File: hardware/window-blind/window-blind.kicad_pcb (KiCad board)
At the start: 2 copper layers, 31 parts, among them IC1 ATMEGA48PA-A, P1 CONN_02X03, SW1 UP, SW2 DN, SW3 END1, SW4 END2, U1 SP3485CN, U2 L298N, U3 LM78L05ACZ, Y1 16M

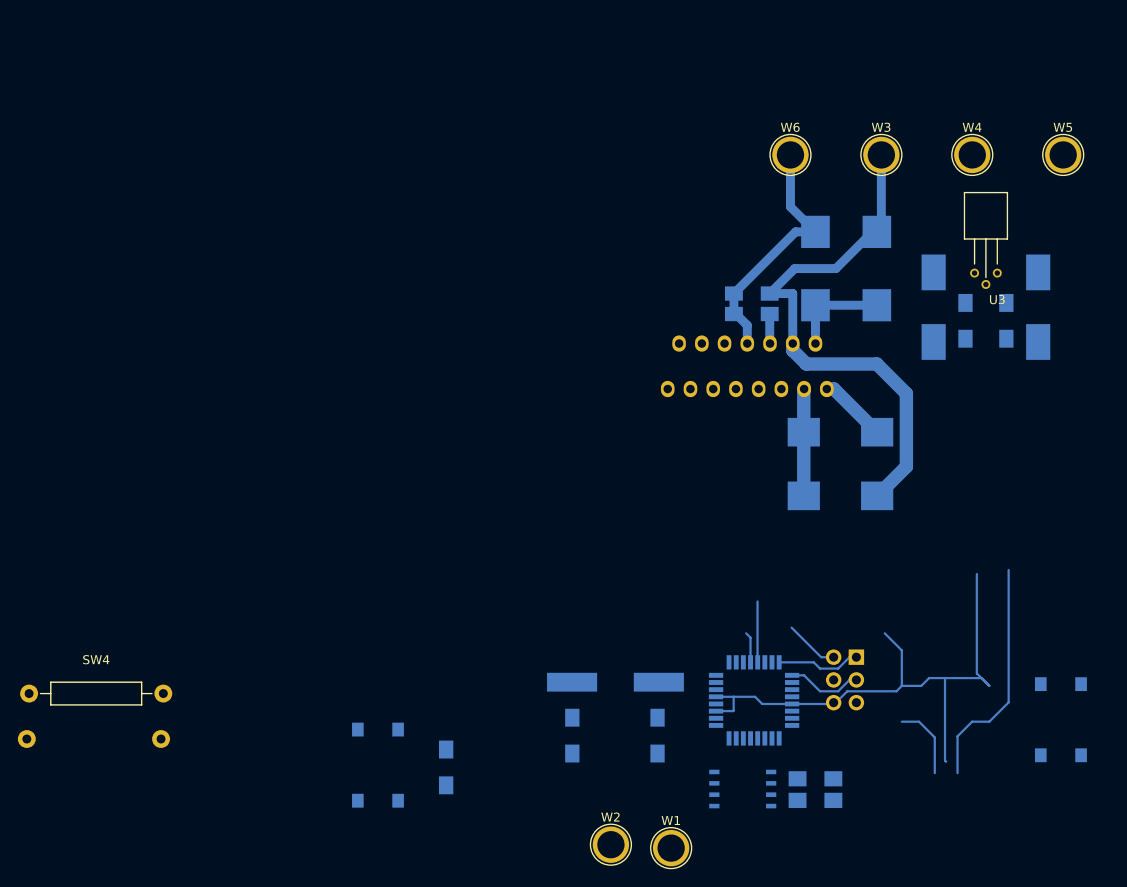
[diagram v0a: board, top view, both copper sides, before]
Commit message: Built sunblind PCB layout
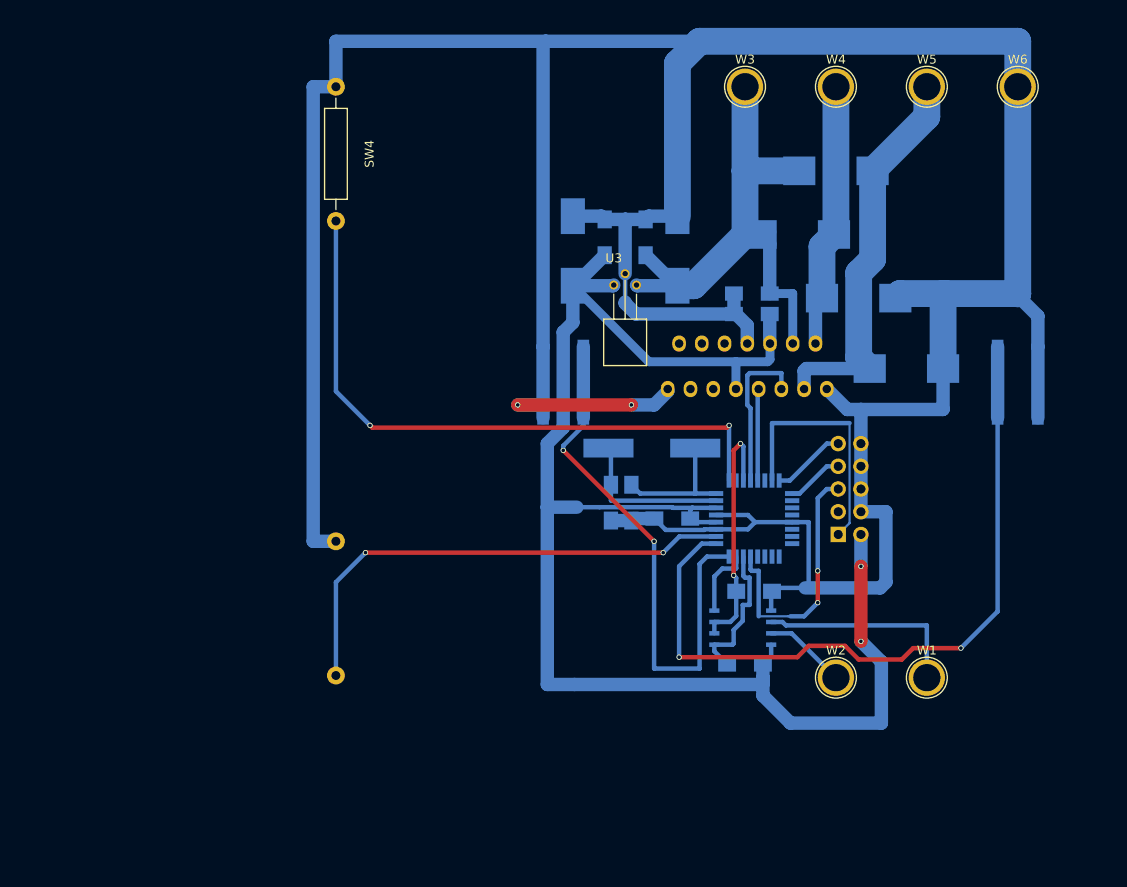
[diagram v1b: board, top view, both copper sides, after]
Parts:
- P1: value CONN_02X03 -> CONN_02X05; footprint Pin_Headers:Pin_Header_Straight_2x03 -> Pin_Headers:Pin_Header_Straight_2x05
- moved SW4 76.0 mm to (142.2, 58.4), turned to 270 degrees
- moved C9 52.4 mm to (168.7, 76.8), turned to 90 degrees
- moved SW2 47.5 mm to (167.6, 91.4), turned to 270 degrees
- moved C8 45.9 mm to (172.3, 75.2), turned to 270 degrees
- moved U3 42.9 mm to (173.3, 80.6), turned to 0 degrees
- moved SW3 41.0 mm to (142.2, 109.2), turned to 270 degrees
- moved SW1 38.0 mm to (218.4, 91.4), turned to 90 degrees
- moved C1 37.6 mm to (179.8, 106.7), turned to 180 degrees
- moved C6 36.9 mm to (176.8, 75.2), turned to 90 degrees
- moved D3 36.3 mm to (198.1, 67.8), turned to 0 degrees
- moved W1 34.3 mm to (208.3, 124.5)
- moved W2 31.3 mm to (198.1, 124.5)
- moved C7 29.3 mm to (180.4, 76.8), turned to 90 degrees
- moved C3 26.9 mm to (175.3, 104.9)
- moved C2 26.6 mm to (173.0, 104.9)
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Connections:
- P1 pad 1: Net-(IC1-Pad16) -> Net-(IC1-Pad15)
- P1 pad 3: Net-(IC1-Pad17) -> Net-(P1-Pad3)
- P1 pad 4: Net-(IC1-Pad15) -> GND
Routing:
- net GND: track 100.8 -> 417.8 mm, vias 0 -> 2
- net +5V: track 9.38 -> 181.3 mm, vias 0 -> 2
- net Net-(IC1-Pad1): track 0.00 -> 83.9 mm, vias 0 -> 2
- net Net-(IC1-Pad9): track 0.00 -> 70.9 mm, vias 0 -> 2
- net Net-(IC1-Pad32): track 0.00 -> 61.5 mm, vias 0 -> 2
- net Net-(IC1-Pad2): track 0.00 -> 55.0 mm, vias 0 -> 2
- net (no net): track 34.6 -> 0.00 mm
- net Net-(D3-Pad2): track 12.0 -> 44.6 mm
- net Net-(IC1-Pad29): track 0.00 -> 29.1 mm, vias 0 -> 2
- net Net-(IC1-Pad15): track 0.00 -> 28.0 mm
- net Net-(IC1-Pad11): track 0.00 -> 28.0 mm, vias 0 -> 2
- net Net-(U1-Pad6): track 0.00 -> 23.4 mm
- net Net-(D1-Pad2): track 11.1 -> 29.6 mm
- net Net-(C2-Pad1): track 0.00 -> 17.7 mm
- net Net-(IC1-Pad30): track 0.00 -> 16.4 mm
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
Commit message: Updated window blind driver PCB to ver. 1.0
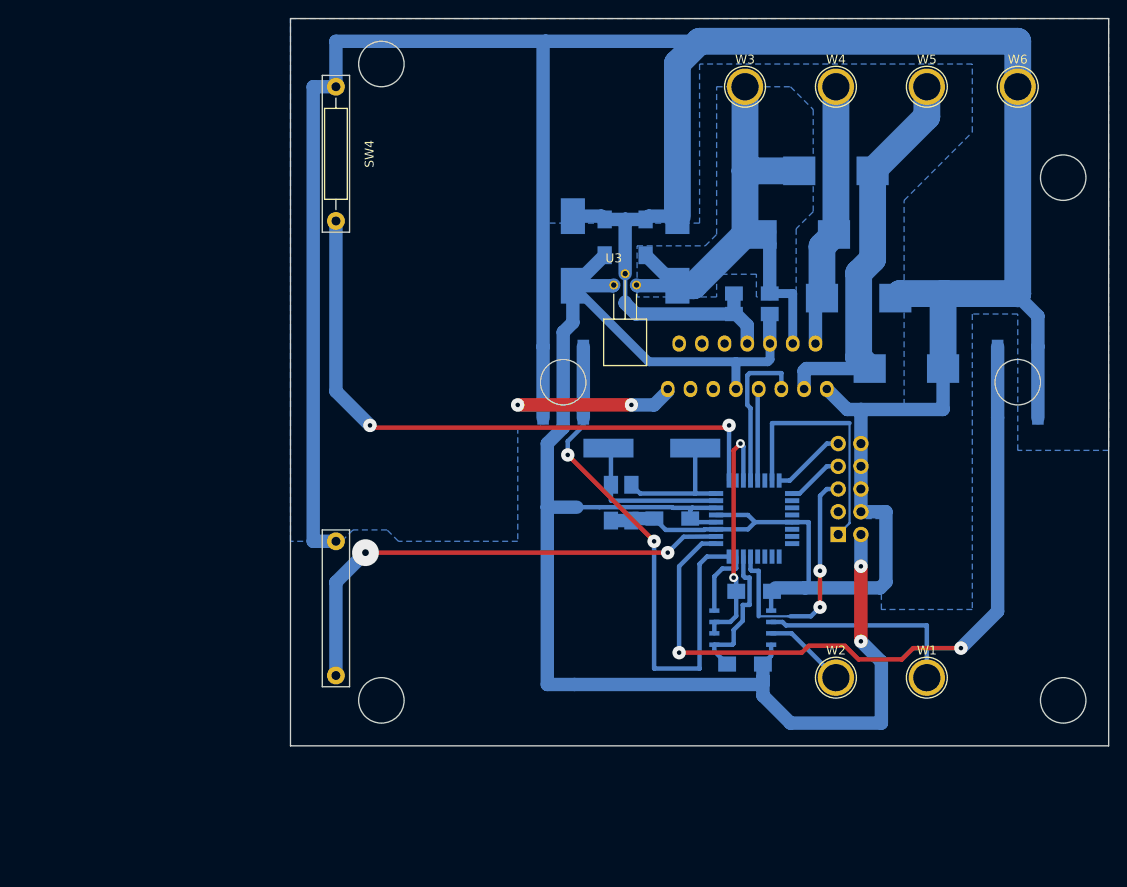
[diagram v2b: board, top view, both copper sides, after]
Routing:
- net Net-(IC1-Pad1): track 83.9 -> 83.2 mm
- added copper zone on B.Cu, net GND
- added copper zone on B.Cu, net Net-(C5-Pad1)
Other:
- board outline added: 91.4 x 81.3 mm
- board text added: "OpenSmartHome Window blind driver ver. 1.0 Copyright (C) 2016 Sergey Portnov License: CC-BY-SA 4.0"

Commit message: Slightly rebuilt PCB, added some functions to use in firmware
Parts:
- added C10: 100, Capacitors_Tantalum_SMD:TantalC_SizeD_EIA-7343_HandSoldering, B.Cu at (183.6, 65.3)
- moved C6 5.28 mm to (182.1, 74.9)
- moved C8 5.18 mm to (167.1, 74.7)
- moved D1 3.06 mm to (194.1, 71.9)
- moved D3 3.05 mm to (198.1, 64.8)
- moved C9 1.81 mm to (170.4, 76.2)
- moved C7 1.69 mm to (178.8, 76.2)
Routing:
- net Net-(C10-Pad1): track 61.1 -> 75.7 mm
- net +5V: track 181.3 -> 178.9 mm
- added copper zone on B.Cu, net Net-(C5-Pad1)
- removed copper zone on B.Cu, net Net-(C10-Pad1)
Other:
- outline, holes or cut-outs redrawn

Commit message: Moved filter capacitors on PCB, rebuilt SVG.
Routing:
- added copper zone on B.Cu, net Net-(C10-Pad1)
- removed copper zone on B.Cu, net Net-(C5-Pad1)
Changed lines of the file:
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@@
     (zones 0)
     (modules 32)
-    (nets 42)
+    (nets 41)
   )
   (page A4)
@@
   )
   (setup
-    (last_trace_width 1.5)
+    (last_trace_width 0.25)
     (user_trace_width 0.25)
     (user_trace_width 0.5)
@@
   (net 37 "Net-(U2-Pad14)")
   (net 38 "Net-(C2-Pad1)")
-  (net 39 "Net-(C5-Pad1)")
-  (net 40 "Net-(P1-Pad3)")
-  (net 41 "Net-(C10-Pad1)")
+  (net 39 "Net-(P1-Pad3)")
+  (net 40 "Net-(C10-Pad1)")
   (net_class Default "Это класс цепей по умолчанию."
     (clearance 0.2)
@@
       (net 5 "Net-(D3-Pad2)"))
     (pad 4 thru_hole oval (at 3.81 5.08 180) (size 1.524 1.824) (drill 0.95) (layers *.Cu *.Mask B.SilkS)
-      (net 41 "Net-(C10-Pad1)"))
+      (net 40 "Net-(C10-Pad1)"))
     (pad 5 thru_hole oval (at 5.08 0 180) (size 1.524 1.824) (drill 0.95) (layers *.Cu *.Mask B.SilkS)
       (net 11 "Net-(IC1-Pad12)"))
@@
     (fp_line (start -1 -1.025) (end 1 -1.025) (layer B.SilkS) (width 0.15))
     (pad 1 smd rect (at -2 0 90) (size 2 1.6) (layers B.Cu B.Paste B.Mask)
-      (net 41 "Net-(C10-Pad1)"))
+      (net 40 "Net-(C10-Pad1)"))
     (pad 2 smd rect (at 2 0 90) (size 2 1.6) (layers B.Cu B.Paste B.Mask)
       (net 2 GND))
@@
       (net 4 "Net-(D1-Pad2)"))
     (pad 1 smd rect (at -4.1 0) (size 3.6 3.2) (layers B.Cu B.Paste B.Mask)
-      (net 41 "Net-(C10-Pad1)"))
+      (net 40 "Net-(C10-Pad1)"))
     (model Diodes_SMD.3dshapes/DO-214AB_Handsoldering.wrl
       (at (xyz 0 0 0))
@@
       (net 5 "Net-(D3-Pad2)"))
     (pad 1 smd rect (at -4.1 0) (size 3.6 3.2) (layers B.Cu B.Paste B.Mask)
-      (net 41 "Net-(C10-Pad1)"))
+      (net 40 "Net-(C10-Pad1)"))
     (model Diodes_SMD.3dshapes/DO-214AB_Handsoldering.wrl
       (at (xyz 0 0 0))
@@
       (net 2 GND))
     (pad 3 thru_hole circle (at 2.54 0 90) (size 1.00076 1.00076) (drill 0.6) (layers *.Cu *.Mask F.SilkS)
-      (net 41 "Net-(C10-Pad1)"))
+      (net 40 "Net-(C10-Pad1)"))
     (pad 1 thru_hole circle (at 0 0 90) (size 1.00076 1.00076) (drill 0.6) (layers *.Cu *.Mask F.SilkS)
       (net 1 +5V))
@@
     (fp_circle (center 0 0) (end 0 -2.286) (layer F.SilkS) (width 0.15))
     (pad 1 thru_hole circle (at 0 0) (size 4.064 4.064) (drill 3.048) (layers *.Cu *.Mask F.SilkS)
-      (net 41 "Net-(C10-Pad1)"))
+      (net 40 "Net-(C10-Pad1)"))
   )
   (module Connect:1pin (layer F.Cu)
@@
     (fp_line (start -1 -1.025) (end 1 -1.025) (layer B.SilkS) (width 0.15))
     (pad 1 smd rect (at -2 0 180) (size 2 1.6) (layers B.Cu B.Paste B.Mask)
-      (net 41 "Net-(C10-Pad1)"))
+      (net 40 "Net-(C10-Pad1)"))
     (pad 2 smd rect (at 2 0 180) (size 2 1.6) (layers B.Cu B.Paste B.Mask)
       (net 2 GND))
@@
       (net 2 GND))
     (pad 1 smd rect (at -3.88874 0 90) (size 4.0005 2.70002) (layers B.Cu B.Paste B.Mask)
-      (net 41 "Net-(C10-Pad1)"))
+      (net 40 "Net-(C10-Pad1)"))
     (model Capacitors_Tantalum_SMD.3dshapes/TantalC_SizeD_EIA-7343_HandSoldering.wrl
       (at (xyz 0 0 0))
@@
       (net 1 +5V))
     (pad 3 thru_hole oval (at 0 -2.54) (size 1.7272 1.7272) (drill 1.016) (layers *.Cu *.Mask B.SilkS)
-      (net 40 "Net-(P1-Pad3)"))
+      (net 39 "Net-(P1-Pad3)"))
     (pad 4 thru_hole oval (at 2.54 -2.54) (size 1.7272 1.7272) (drill 1.016) (layers *.Cu *.Mask B.SilkS)
       (net 2 GND))
@@
       (net 2 GND))
     (pad 1 smd rect (at -3.88874 0 180) (size 4.0005 2.70002) (layers B.Cu B.Paste B.Mask)
-      (net 41 "Net-(C10-Pad1)"))
+      (net 40 "Net-(C10-Pad1)"))
     (model Capacitors_Tantalum_SMD.3dshapes/TantalC_SizeD_EIA-7343_HandSoldering.wrl
       (at (xyz 0 0 0))
@@
   (segment (start 172.974 104.648) (end 172.974 102.902) (width 0.5) (layer B.Cu) (net 38))
   (segment (start 173.006 104.68) (end 172.974 104.648) (width 0.5) (layer B.Cu) (net 38))
-  (segment (start 178.816 80.08874) (end 179.832 80.08874) (width 1.5) (layer B.Cu) (net 41) (status C00000))
-  (segment (start 179.832 80.08874) (end 180.4035 80.66024) (width 1.5) (layer B.Cu) (net 41) (status 400000))
-  (segment (start 182.118 76.93) (end 182.118 80.54848) (width 1.5) (layer B.Cu) (net 41) (status 400000))
-  (segment (start 182.118 80.54848) (end 182.22976 80.66024) (width 1.5) (layer B.Cu) (net 41))
-  (segment (start 189.956 71.882) (end 189.956 76.926) (width 3) (layer B.Cu) (net 41) (status 400000))
-  (segment (start 189.956 76.926) (end 190.722 77.692) (width 3) (layer B.Cu) (net 41))
-  (segment (start 187.53074 65.278) (end 193.512 65.278) (width 3) (layer B.Cu) (net 41) (status C00000))
-  (segment (start 193.512 65.278) (end 194.02 64.77) (width 3) (layer B.Cu) (net 41) (status C00000))
-  (segment (start 187.96 58.42) (end 187.96 64.84874) (width 3) (layer B.Cu) (net 41) (status C00000))
-  (segment (start 187.96 64.84874) (end 187.53074 65.278) (width 3) (layer B.Cu) (net 41) (status C00000))
-  (segment (start 182.22976 80.66024) (end 187.96 74.93) (width 1.5) (layer B.Cu) (net 41))
-  (segment (start 180.4035 80.66024) (end 182.22976 80.66024) (width 1.5) (layer B.Cu) (net 41))
-  (segment (start 180.4035 80.66024) (end 175.91024 80.66024) (width 1.5) (layer B.Cu) (net 41))
-  (segment (start 187.96 67.818) (end 187.96 74.93) (width 3) (layer B.Cu) (net 41))
-  (segment (start 190.722 74.64) (end 190.21 74.64) (width 1.5) (layer B.Cu) (net 41))
-  (segment (start 190.722 81.534) (end 190.722 77.692) (width 1.5) (layer B.Cu) (net 41))
-  (segment (start 190.722 77.692) (end 190.722 75.95) (width 1.5) (layer B.Cu) (net 41))
-  (segment (start 187.96 74.93) (end 189.702 74.93) (width 3) (layer B.Cu) (net 41))
-  (segment (start 187.96 74.93) (end 189.702 74.93) (width 3) (layer B.Cu) (net 41))
-  (segment (start 190.722 75.95) (end 189.702 74.93) (width 1.5) (layer B.Cu) (net 41))
-  (segment (start 187.96 58.42) (end 187.96 67.818) (width 3) (layer B.Cu) (net 41))
-  (segment (start 175.91024 80.66024) (end 175.8315 80.5815) (width 1.5) (layer B.Cu) (net 41))
-  (segment (start 193.294 87.122) (end 193.294 81.534) (width 1) (layer B.Cu) (net 41))
-  (segment (start 193.294 81.534) (end 190.722 81.534) (width 1) (layer B.Cu) (net 41))
+  (segment (start 178.816 80.08874) (end 179.832 80.08874) (width 1.5) (layer B.Cu) (net 40))
+  (segment (start 179.832 80.08874) (end 180.4035 80.66024) (width 1.5) (layer B.Cu) (net 40))
+  (segment (start 182.118 76.93) (end 182.118 80.54848) (width 1.5) (layer B.Cu) (net 40))
+  (segment (start 182.118 80.54848) (end 182.22976 80.66024) (width 1.5) (layer B.Cu) (net 40))
+  (segment (start 189.956 71.882) (end 189.956 76.926) (width 3) (layer B.Cu) (net 40))
+  (segment (start 189.956 76.926) (end 190.722 77.692) (width 3) (layer B.Cu) (net 40))
+  (segment (start 187.53074 65.278) (end 193.512 65.278) (width 3) (layer B.Cu) (net 40))
+  (segment (start 193.512 65.278) (end 194.02 64.77) (width 3) (layer B.Cu) (net 40))
+  (segment (start 187.96 58.42) (end 187.96 64.84874) (width 3) (layer B.Cu) (net 40))
+  (segment (start 187.96 64.84874) (end 187.53074 65.278) (width 3) (layer B.Cu) (net 40))
+  (segment (start 182.22976 80.66024) (end 187.96 74.93) (width 1.5) (layer B.Cu) (net 40))
+  (segment (start 180.4035 80.66024) (end 182.22976 80.66024) (width 1.5) (layer B.Cu) (net 40))
+  (segment (start 180.4035 80.66024) (end 175.91024 80.66024) (width 1.5) (layer B.Cu) (net 40))
+  (segment (start 187.96 67.818) (end 187.96 74.93) (width 3) (layer B.Cu) (net 40))
+  (segment (start 190.722 74.64) (end 190.21 74.64) (width 1.5) (layer B.Cu) (net 40))
+  (segment (start 190.722 81.534) (end 190.722 77.692) (width 1.5) (layer B.Cu) (net 40))
+  (segment (start 190.722 77.692) (end 190.722 75.95) (width 1.5) (layer B.Cu) (net 40))
+  (segment (start 187.96 74.93) (end 189.702 74.93) (width 3) (layer B.Cu) (net 40))
+  (segment (start 187.96 74.93) (end 189.702 74.93) (width 3) (layer B.Cu) (net 40))
+  (segment (start 190.722 75.95) (end 189.702 74.93) (width 1.5) (layer B.Cu) (net 40))
+  (segment (start 187.96 58.42) (end 187.96 67.818) (width 3) (layer B.Cu) (net 40))
+  (segment (start 175.91024 80.66024) (end 175.8315 80.5815) (width 1.5) (layer B.Cu) (net 40))
+  (segment (start 193.294 87.122) (end 193.294 81.534) (width 1) (layer B.Cu) (net 40))
+  (segment (start 193.294 81.534) (end 190.722 81.534) (width 1) (layer B.Cu) (net 40))
   (zone (net 2) (net_name GND) (layer B.Cu) (hatch edge 0.508)
     (connect_pads thru_hole_only (clearance 0.508))
@@
     )
   )
-  (zone (net 39) (net_name "Net-(C5-Pad1)") (layer B.Cu) (hatch edge 0.508)
+  (zone (net 40) (net_name "Net-(C10-Pad1)") (layer B.Cu) (hatch edge 0.508)
     (connect_pads thru_hole_only (clearance 0.508))
     (min_thickness 0.254)
